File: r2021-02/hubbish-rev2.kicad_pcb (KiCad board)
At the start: 4 copper layers, 100 x 100 mm, 123 parts, among them J1 Conn_01x06, J2 USB_A_Stacked, J3 USB_A_Stacked, J4 USB_A (female down), J5 Conn_01x03_Male, J6 USB_A_Stacked, J8 USB_A male UP, J9 USB_B_Micro (up), Q1 Si4435, U1 2k i2c eeprom, U10 NUP4202, U11 NUP4202, U12 NUP4202, U13 NUP4202, U14 NUP4202, U15 NUP4202, U16 NUP4202, U17 NUP4202, U18 SE5120ST33, U19 APL3511C, U2 SiC437AED, U3 USB2517, U4 APL3511C, U5 APL3511C, U6 APL3511C, U7 APL3511C, U8 APL3511C, U9 APL3511C, Y1 24MHz

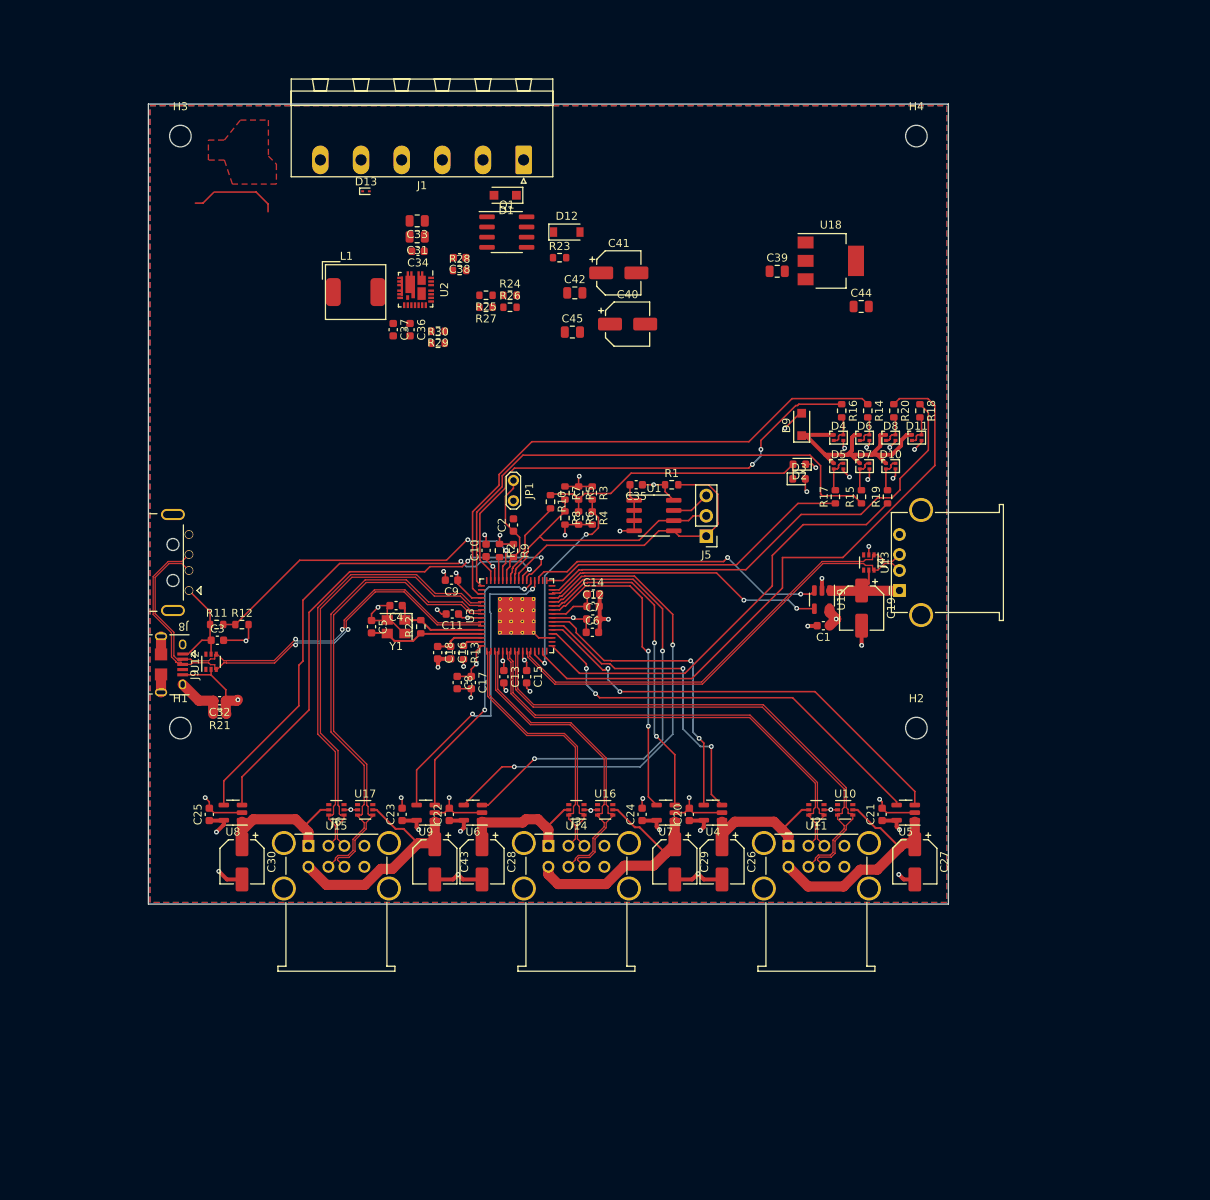
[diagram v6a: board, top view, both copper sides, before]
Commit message: restore to kicad 6.0 compatibility
updated to my footprintbranch, 6.0 and all that
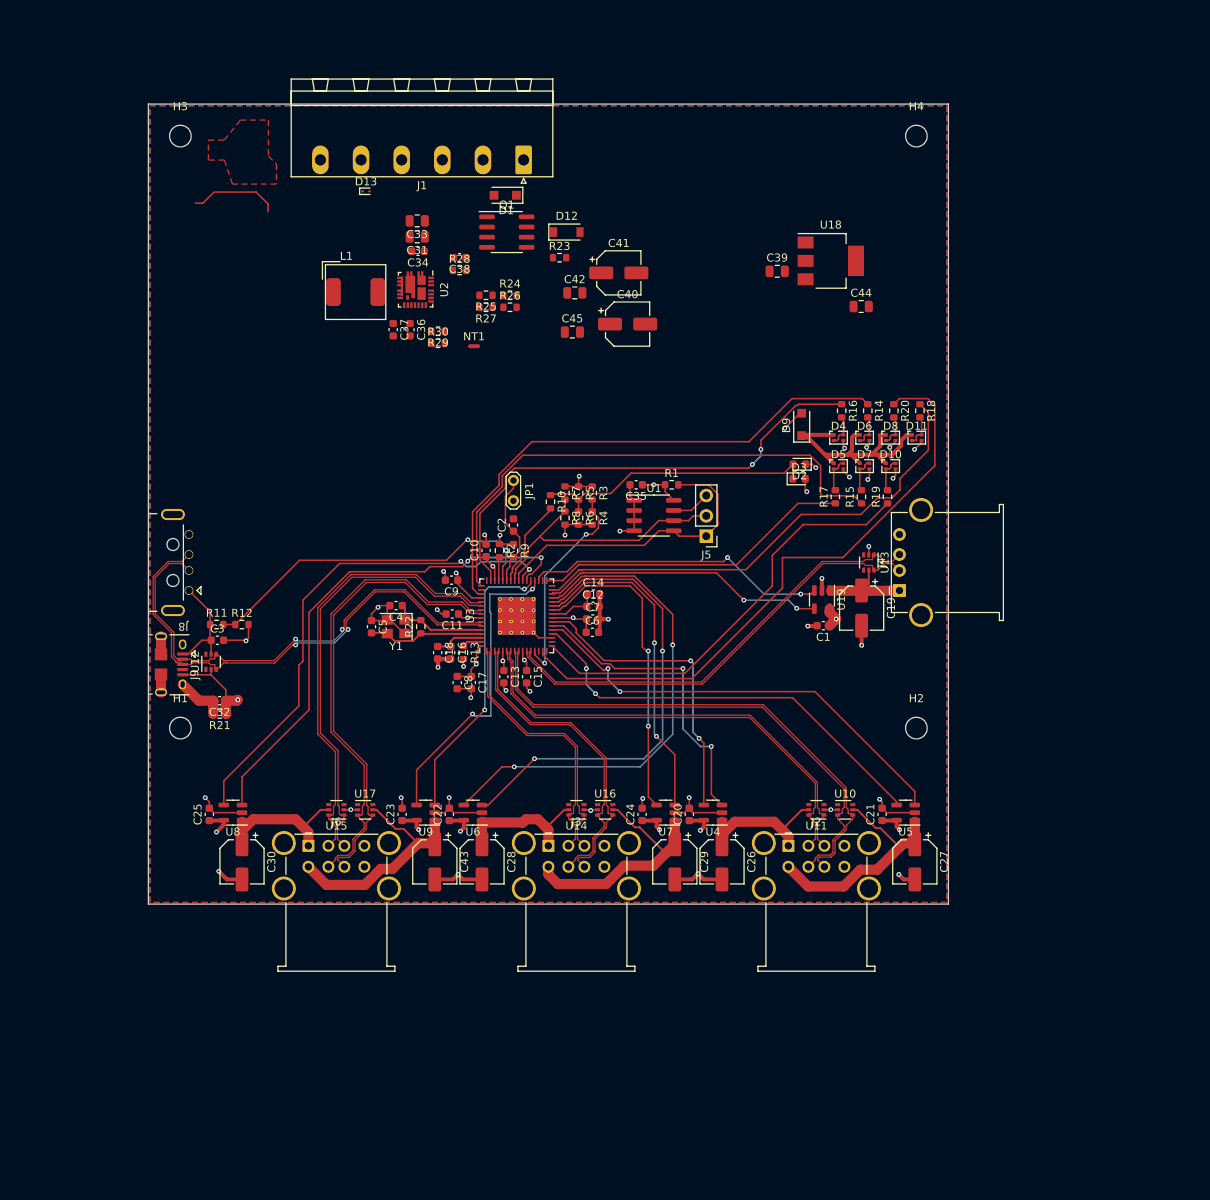
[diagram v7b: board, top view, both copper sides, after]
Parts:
- added NT1: NetTie_2, NetTie:NetTie-2_SMD_Pad0.5mm, F.Cu at (120.7, 80.3)

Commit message: hubbish-r2: shrink to 100x80
re-connect all the parts, and continue to shirk responsibilities to
route the power supply again.
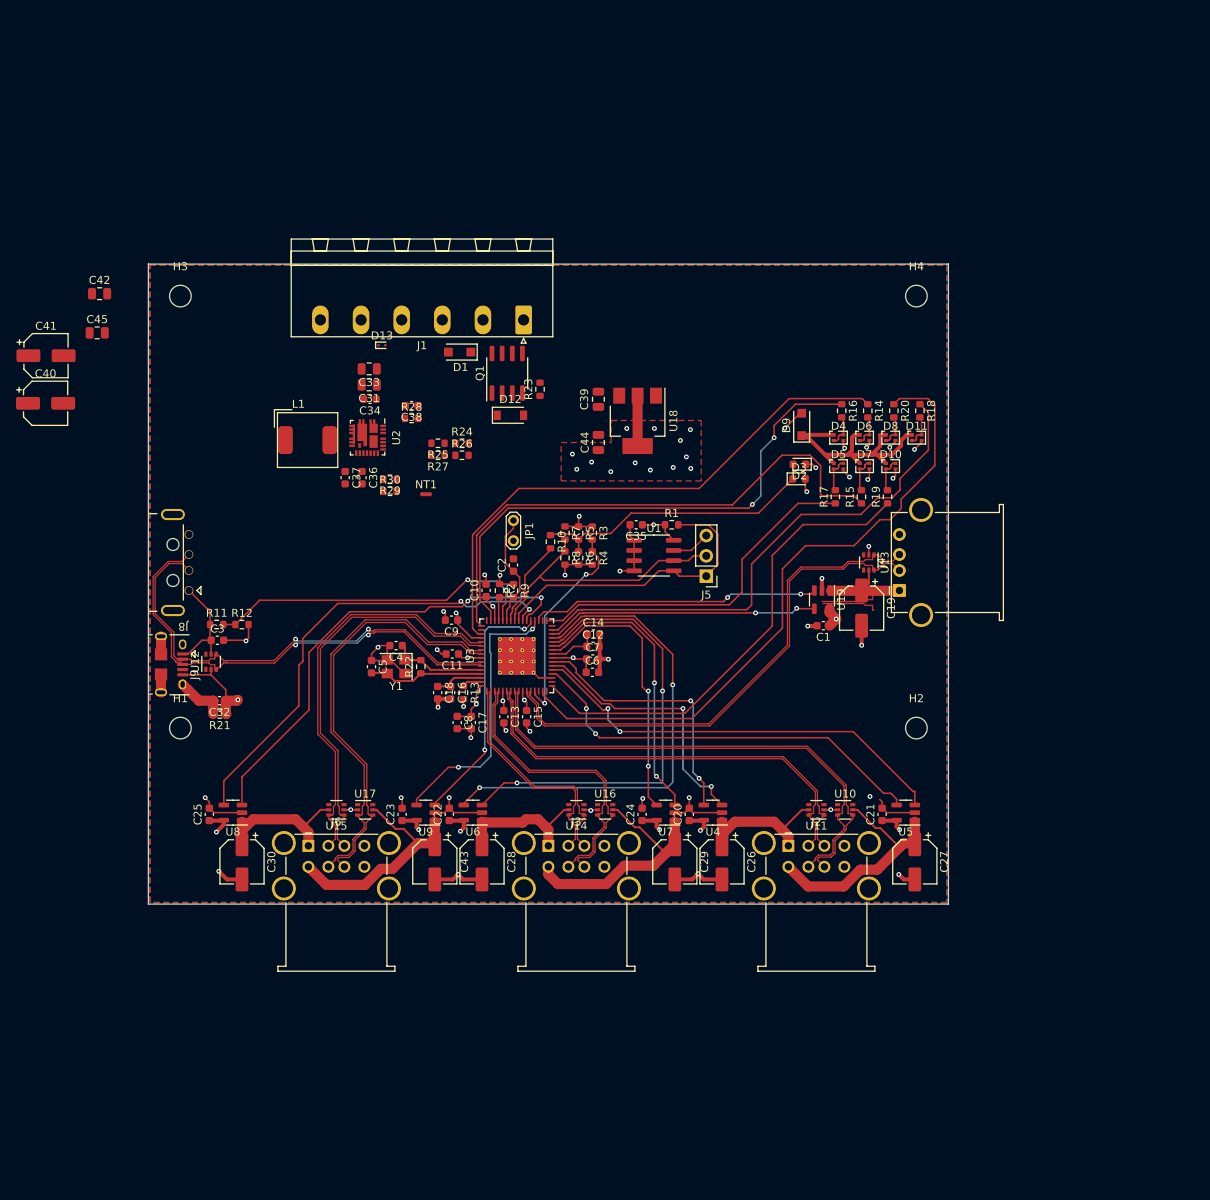
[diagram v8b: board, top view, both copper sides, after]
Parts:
- moved C40 73.4 mm to (67.2, 87.4)
- moved C41 72.3 mm to (67.2, 81.5)
- moved C42 59.4 mm to (73.9, 73.7)
- moved C45 59.4 mm to (73.6, 78.6)
- moved C44 37.0 mm to (136.2, 92.3), turned to 90 degrees
- moved U18 31.4 mm to (141.2, 89.6), turned to -90 degrees
- moved C39 27.5 mm to (136.2, 86.9), turned to -90 degrees
- moved D12 24.0 mm to (125.2, 88.9)
- moved D1 20.4 mm to (118.9, 81.0)
- moved J1 20.0 mm to (126.9, 77.0)
- moved H3 20.0 mm to (84.0, 74.0)
- moved H4 20.0 mm to (176.0, 74.0)
- moved C31 19.4 mm to (107.6, 85.1)
- moved C33 19.4 mm to (107.6, 83.1)
- moved C34 19.4 mm to (107.7, 86.9)
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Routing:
- net (no net): track 11.1 -> 0.00 mm
- net /downstream-port-power/DS-: track 56.3 -> 64.2 mm
- net /downstream-port-power/DS+: track 55.9 -> 63.8 mm
- net /downstream-port-power/VBUS_DS: track 11.5 -> 18.6 mm
- net +5V: track 43.7 -> 50.7 mm, vias 7 -> 8
- net +3V3: track 46.3 -> 52.6 mm, vias 12 -> 25
- net /upstream-config-leds/LED_A3: track 61.8 -> 67.3 mm
- net /upstream-config-leds/LED_A5: track 61.3 -> 66.4 mm
- net /downstream-port-power/U5+: track 55.1 -> 50.1 mm
- net /downstream-port-power/OC6: track 36.1 -> 31.1 mm
- net /upstream-config-leds/LED_A6: track 54.4 -> 59.4 mm
- net /downstream-port-power/U6-: track 59.1 -> 54.1 mm
- net /downstream-port-power/OC5: track 63.2 -> 58.2 mm
- net /downstream-port-power/EN1: track 38.4 -> 33.4 mm
- net /downstream-port-power/U6+: track 58.5 -> 53.5 mm
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- added copper zone on F.Cu, net +3V3
- removed copper zone on F.Cu, net (none)
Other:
- board size 100 x 100 mm -> 100 x 80 mm
